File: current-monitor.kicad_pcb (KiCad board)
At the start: 4 copper layers, 70 x 58.2 mm, 152 parts, among them J201 CONN-3, J601 USB-MICROB, J602 SWD, J603 CONN-6, K201 RELAY-DPDT-EE2-SPLIT, K202 RELAY-DPDT-EE2-SPLIT, Q201 DRDC3105E6, U201 FSA1259A, U202 MAX4737EUD, U301 AD8429A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

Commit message: adjust mask clearance
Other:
- rule pad_to_mask_clearance: 0 -> 0.1
- board text added: "IN"
- board text added: "OUT"
- board text added: "sternlabs"
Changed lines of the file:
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@@
     (links 332)
     (no_connects 0)
-    (area 90.949999 59.949999 161.050001 118.250001)
+    (area 90.949999 59.949999 162.774001 118.250001)
     (thickness 1.6)
-    (drawings 8)
+    (drawings 14)
     (tracks 1240)
     (zones 0)
@@
     (zone_45_only no)
     (trace_min 0.15)
-    (segment_width 0.2)
+    (segment_width 0.3)
     (edge_width 0.1)
     (via_size 0.6)
@@
     (pad_size 1.5 0.3)
     (pad_drill 0)
-    (pad_to_mask_clearance 0)
+    (pad_to_mask_clearance 0.1)
+    (solder_mask_min_width 0.1)
     (aux_axis_origin 0 0)
     (visible_elements FFFFFF7F)
@@
       (net 2 COM))
   )
+  (gr_text sternlabs (at 98.6 116.2) (layer F.SilkS)
+    (effects (font (size 1.5 1.5) (thickness 0.15)))
+  )
+  (gr_line (start 92.4 70.8) (end 92.4 71.2) (layer F.SilkS) (width 0.3))
+  (gr_line (start 93 70.4) (end 93 71.6) (layer F.SilkS) (width 0.3))
+  (gr_line (start 93.6 70) (end 93.6 72) (layer F.SilkS) (width 0.3))
+  (gr_text OUT (at 93 74.8 270) (layer F.SilkS)
+    (effects (font (size 1.5 1.5) (thickness 0.3)))
+  )
+  (gr_text IN (at 93.2 67.6 270) (layer F.SilkS)
+    (effects (font (size 1.5 1.5) (thickness 0.3)))
+  )
   (gr_line (start 91 60) (end 91 118.2) (layer Edge.Cuts) (width 0.1))
   (gr_line (start 161 60) (end 91 60) (layer Edge.Cuts) (width 0.1))
@@
     (polygon
       (pts
-        (xy 91 60) (xy 161 60) (xy 161 118.2) (xy 91 118.4)
+        (xy 91 60) (xy 161 60) (xy 161 118.2) (xy 91 118.2)
       )
     )
@@
     (polygon
       (pts
-        (xy 148.2 110.4) (xy 143.6 105.8) (xy 143.6 104.2) (xy 147.6 104.2) (xy 150.6 109.4)
-        (xy 150.6 110.4)
+        (xy 149.6 110.4) (xy 143.6 105.8) (xy 143.6 103.4) (xy 147.6 103.4) (xy 151.8 109)
+        (xy 151.8 110.4)
       )
     )
@@
     (polygon
       (pts
-        (xy 91 60.025214) (xy 161 60.025214) (xy 161 118.225214) (xy 91 118.425214)
+        (xy 91 60) (xy 161 60) (xy 161 118.2) (xy 91 118.2)
       )
     )
@@
     (polygon
       (pts
-        (xy 90.959971 60) (xy 160.959971 60) (xy 160.959971 118.2) (xy 90.959971 118.4)
+        (xy 91 60) (xy 161 60) (xy 161 118.2) (xy 91 118.2)
       )
     )

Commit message: zone connections
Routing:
- net COM: track 111.3 -> 114.9 mm
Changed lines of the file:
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@@
     (thickness 1.6)
     (drawings 14)
-    (tracks 1240)
+    (tracks 1244)
     (zones 0)
     (modules 152)
@@
       (net 12 +3.00V))
     (pad 15 smd rect (at -5.7 3.25) (size 1.5 0.3) (layers F.Cu F.Paste F.Mask)
-      (net 2 COM))
+      (net 2 COM) (zone_connect 1))
     (pad 16 smd rect (at -5.7 3.75) (size 1.5 0.3) (layers F.Cu F.Paste F.Mask)
-      (net 2 COM))
+      (net 2 COM) (zone_connect 1))
     (pad 17 smd rect (at -3.75 5.7 90) (size 1.5 0.3) (layers F.Cu F.Paste F.Mask))
     (pad 18 smd rect (at -3.25 5.7 90) (size 1.5 0.3) (layers F.Cu F.Paste F.Mask)
@@
       (net 78 "Net-(R205-Pad2)"))
     (pad 9 smd rect (at 1.3 -3 90) (size 0.4 1.8) (layers F.Cu F.Paste F.Mask)
-      (net 2 COM))
+      (net 2 COM) (zone_connect 1))
     (pad 10 smd rect (at 0.65 -3 90) (size 0.4 1.8) (layers F.Cu F.Paste F.Mask)
-      (net 2 COM))
+      (net 2 COM) (zone_connect 1))
     (pad 11 smd rect (at 0 -3 90) (size 0.4 1.8) (layers F.Cu F.Paste F.Mask)
       (net 77 "Net-(R204-Pad2)"))
@@
   (segment (start 102.75 87.8) (end 102.5 87.55) (width 0.4) (layer F.Cu) (net 1) (status 30))
   (segment (start 102.5 85.25) (end 103.05 84.7) (width 0.4) (layer F.Cu) (net 1) (status 30))
+  (segment (start 145.8 66.7) (end 144.468202 66.7) (width 0.4) (layer F.Cu) (net 2))
+  (segment (start 144.468202 66.7) (end 144.168202 67) (width 0.4) (layer F.Cu) (net 2))
+  (segment (start 145.8 67.35) (end 144.5 67.35) (width 0.4) (layer F.Cu) (net 2))
+  (segment (start 144.5 67.35) (end 144.15 67) (width 0.4) (layer F.Cu) (net 2))
+  (segment (start 145.8 67.35) (end 146.95 67.35) (width 0.4) (layer F.Cu) (net 2))
+  (segment (start 146.95 67.35) (end 147 67.4) (width 0.4) (layer F.Cu) (net 2))
+  (segment (start 145.8 66.7) (end 146.9 66.7) (width 0.4) (layer F.Cu) (net 2))
+  (segment (start 146.9 66.7) (end 147 66.8) (width 0.4) (layer F.Cu) (net 2))
   (segment (start 140.3 97.5) (end 140.3 98.3) (width 0.2) (layer F.Cu) (net 2))
   (segment (start 140.3 98.3) (end 140.2 98.4) (width 0.2) (layer F.Cu) (net 2))
@@
   (segment (start 138.8 65.4) (end 139.6 65.4) (width 0.5) (layer F.Cu) (net 2) (status 10))
   (via (at 139.6 65.4) (size 0.6) (drill 0.3) (layers F.Cu B.Cu) (net 2))
-  (segment (start 145.8 66.7) (end 146.9 66.7) (width 0.3) (layer F.Cu) (net 2) (status 10))
-  (segment (start 146.9 66.7) (end 147 66.8) (width 0.3) (layer F.Cu) (net 2))
   (via (at 147 66.8) (size 0.6) (drill 0.3) (layers F.Cu B.Cu) (net 2))
-  (segment (start 145.8 67.35) (end 146.95 67.35) (width 0.3) (layer F.Cu) (net 2) (status 10))
-  (segment (start 146.95 67.35) (end 147 67.4) (width 0.3) (layer F.Cu) (net 2))
   (via (at 147 67.4) (size 0.6) (drill 0.3) (layers F.Cu B.Cu) (net 2))
   (segment (start 151.8 66.05) (end 150.65 66.05) (width 0.3) (layer F.Cu) (net 2) (status 10))
@@
   (segment (start 131.7 71.273) (end 131.71 71.283) (width 1) (layer F.Cu) (net 73) (status 30))
   (segment (start 131.71 70.338) (end 131.71 71.283) (width 1) (layer F.Cu) (net 73) (status 30))
+  (segment (start 99.8 74.5) (end 100.1 74.5) (width 1) (layer F.Cu) (net 74))
+  (segment (start 100.1 74.5) (end 102.8 71.8) (width 1) (layer F.Cu) (net 74))
+  (segment (start 106.865999 69.083999) (end 109.065 71.283) (width 1) (layer F.Cu) (net 74))
+  (segment (start 102.8 71.8) (end 102.8 70.709798) (width 1) (layer F.Cu) (net 74))
+  (segment (start 102.8 70.709798) (end 104.425799 69.083999) (width 1) (layer F.Cu) (net 74))
+  (segment (start 104.425799 69.083999) (end 106.865999 69.083999) (width 1) (layer F.Cu) (net 74))
   (segment (start 106.2 75.2) (end 106 75.4) (width 0.5) (layer F.Cu) (net 74))
   (segment (start 107.8 75.2) (end 106.2 75.2) (width 0.5) (layer F.Cu) (net 74))
@@
   (segment (start 103.5 71.1) (end 100.1 74.5) (width 1) (layer B.Cu) (net 74))
   (segment (start 100.1 74.5) (end 99.8 74.5) (width 1) (layer B.Cu) (net 74))
-  (segment (start 99.8 74.5) (end 100.1 74.5) (width 1) (layer F.Cu) (net 74))
-  (segment (start 100.1 74.5) (end 102.1 72.5) (width 1) (layer F.Cu) (net 74))
-  (segment (start 102.1 72.5) (end 102.1 71.409798) (width 1) (layer F.Cu) (net 74))
-  (segment (start 104.425799 69.083999) (end 106.865999 69.083999) (width 1) (layer F.Cu) (net 74))
-  (segment (start 102.1 71.409798) (end 104.425799 69.083999) (width 1) (layer F.Cu) (net 74))
   (segment (start 129.4 74) (end 129.4 71.513) (width 0.5) (layer F.Cu) (net 74))
   (segment (start 129.4 71.513) (end 129.17 71.283) (width 0.5) (layer F.Cu) (net 74))
   (segment (start 129.1 69.2) (end 127.2 71.1) (width 1) (layer B.Cu) (net 74))
-  (segment (start 106.865999 69.083999) (end 109.065 71.283) (width 1) (layer F.Cu) (net 74))
   (segment (start 109.065 71.283) (end 110.62 71.283) (width 1) (layer F.Cu) (net 74) (status 20))
   (segment (start 129.17 71.283) (end 129.17 69.27) (width 1) (layer F.Cu) (net 74) (status 10))
@@
     (connect_pads yes (clearance 0.2))
     (min_thickness 0.254)
-    (fill yes (arc_segments 32) (thermal_gap 0.508) (thermal_bridge_width 0.508))
+    (fill yes (arc_segments 32) (thermal_gap 0.2) (thermal_bridge_width 0.508))
     (polygon
       (pts

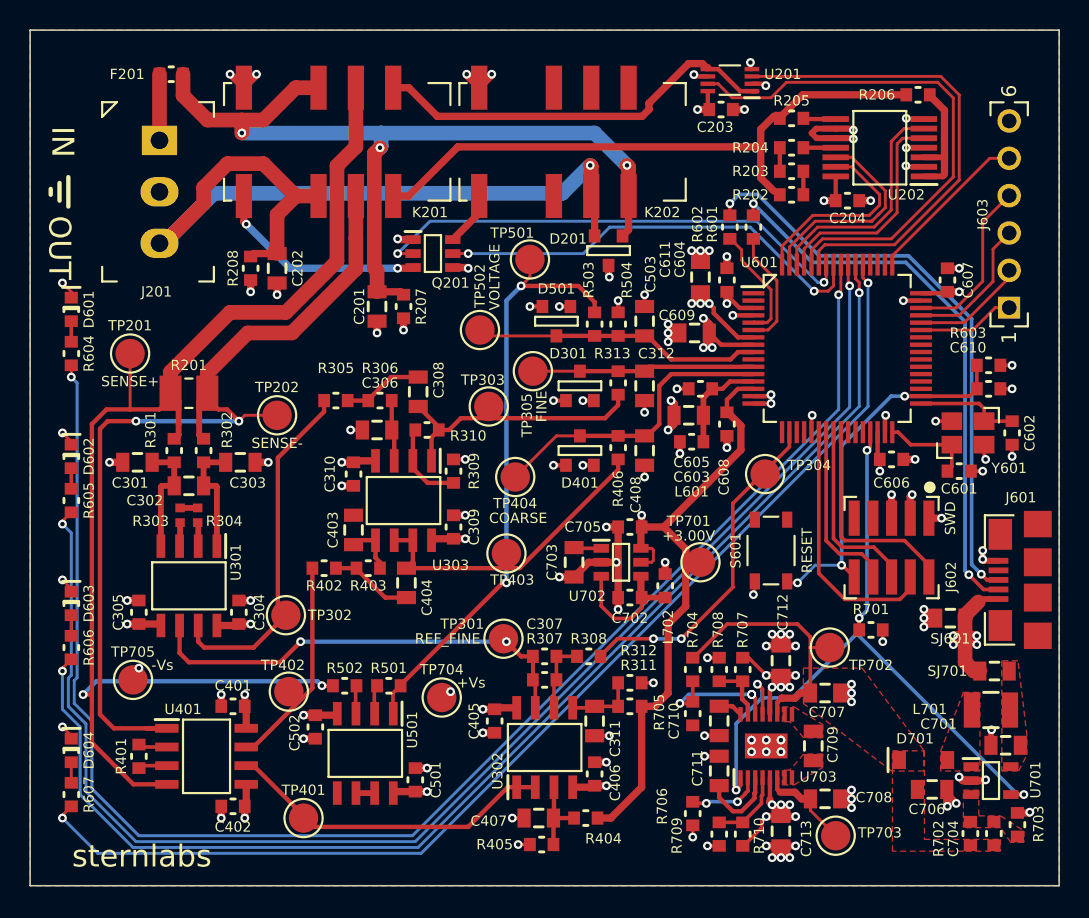
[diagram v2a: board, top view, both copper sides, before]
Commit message: move Q201 to the east
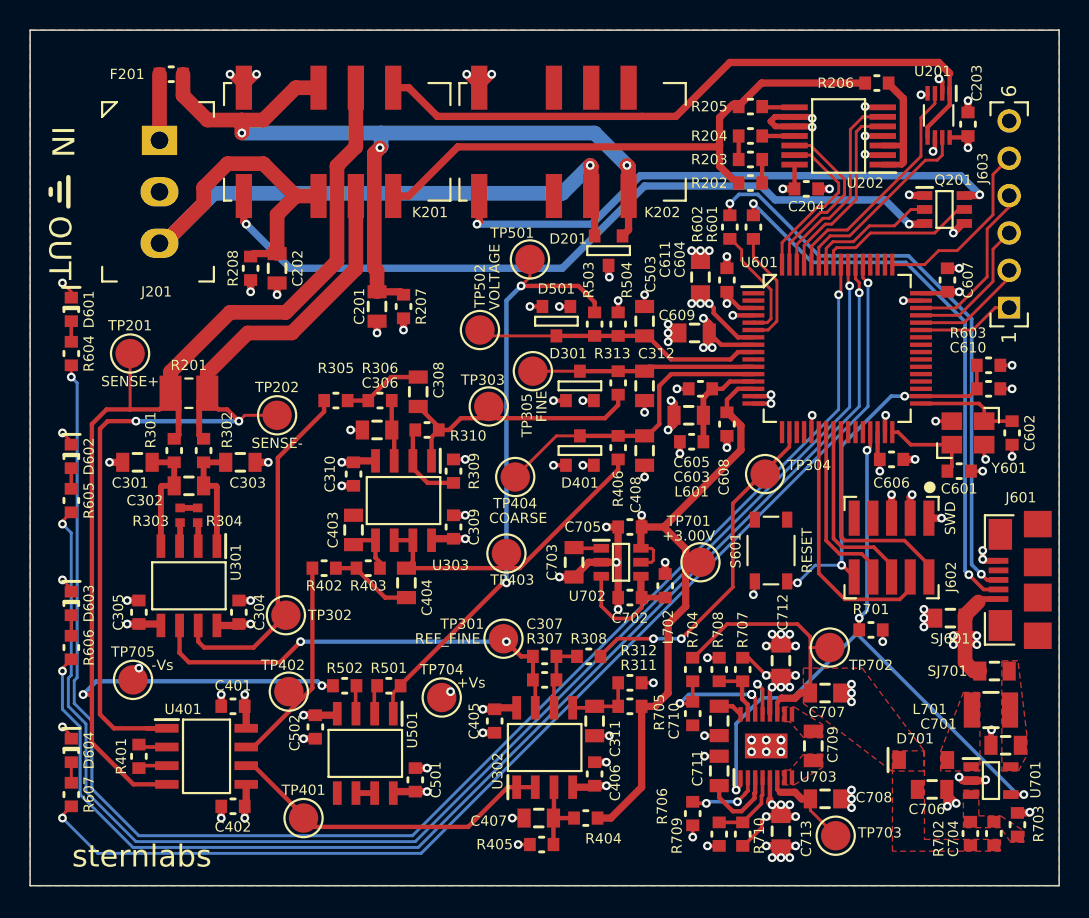
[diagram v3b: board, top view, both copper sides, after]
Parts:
- moved Q201 34.9 mm to (153.2, 72.2)
- moved C203 16.8 mm to (154.8, 66.4), turned to 180 degrees
- moved U201 14.4 mm to (152.8, 65.8), turned to 180 degrees
- moved R206 2.91 mm to (148.6, 63.6)
- moved R202 2.91 mm to (140.0, 70.4)
- moved R203 2.91 mm to (140.0, 68.8)
- moved R204 2.91 mm to (140.0, 67.2)
- moved R205 2.91 mm to (140.0, 65.2)
- moved U202 2.91 mm to (146.0, 67.2)
- moved C204 2.91 mm to (143.8, 70.8)
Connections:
- U601 pad 59: /In/Out, Shunt, Calibration/CALIBRATE_3V -> /In/Out, Shunt, Calibration/CALIBRATE_5V
- U601 pad 60: /In/Out, Shunt, Calibration/CALIBRATE_5V -> /In/Out, Shunt, Calibration/CALIBRATE_3V
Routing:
- net Net-(K201-Pad12): track 14.6 -> 52.8 mm
- net Net-(K202-Pad12): track 3.71 -> 39.2 mm, vias 0 -> 2
- net /In/Out, Shunt, Calibration/RELAY_CALIBRATE: track 34.0 -> 8.90 mm, vias 2 -> 0
- net /In/Out, Shunt, Calibration/CALIBRATE_5V: track 36.1 -> 13.4 mm
- net /In/Out, Shunt, Calibration/RELAY_INOUT_SHORT: track 30.0 -> 11.0 mm, vias 2 -> 0
- net Net-(K201-Pad5): track 28.4 -> 46.2 mm
- net /In/Out, Shunt, Calibration/CALIBRATE_3V: track 32.9 -> 15.9 mm
- net +5V: track 54.1 -> 39.4 mm
- net +3.00V: track 91.0 -> 101.9 mm
- net +3V3: track 107.7 -> 101.2 mm
- net Net-(K201-Pad8): track 41.7 -> 38.9 mm
- net /In/Out, Shunt, Calibration/CALIBRATE_3uA: track 14.4 -> 12.0 mm
- net /In/Out, Shunt, Calibration/CALIBRATE_300uA: track 15.9 -> 13.5 mm
- net /In/Out, Shunt, Calibration/CALIBRATE_30mA_2: track 15.1 -> 12.7 mm
- net /In/Out, Shunt, Calibration/CALIBRATE_30mA: track 13.5 -> 11.2 mm
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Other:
- rule pad_to_mask_clearance: 0.1 -> 0.049

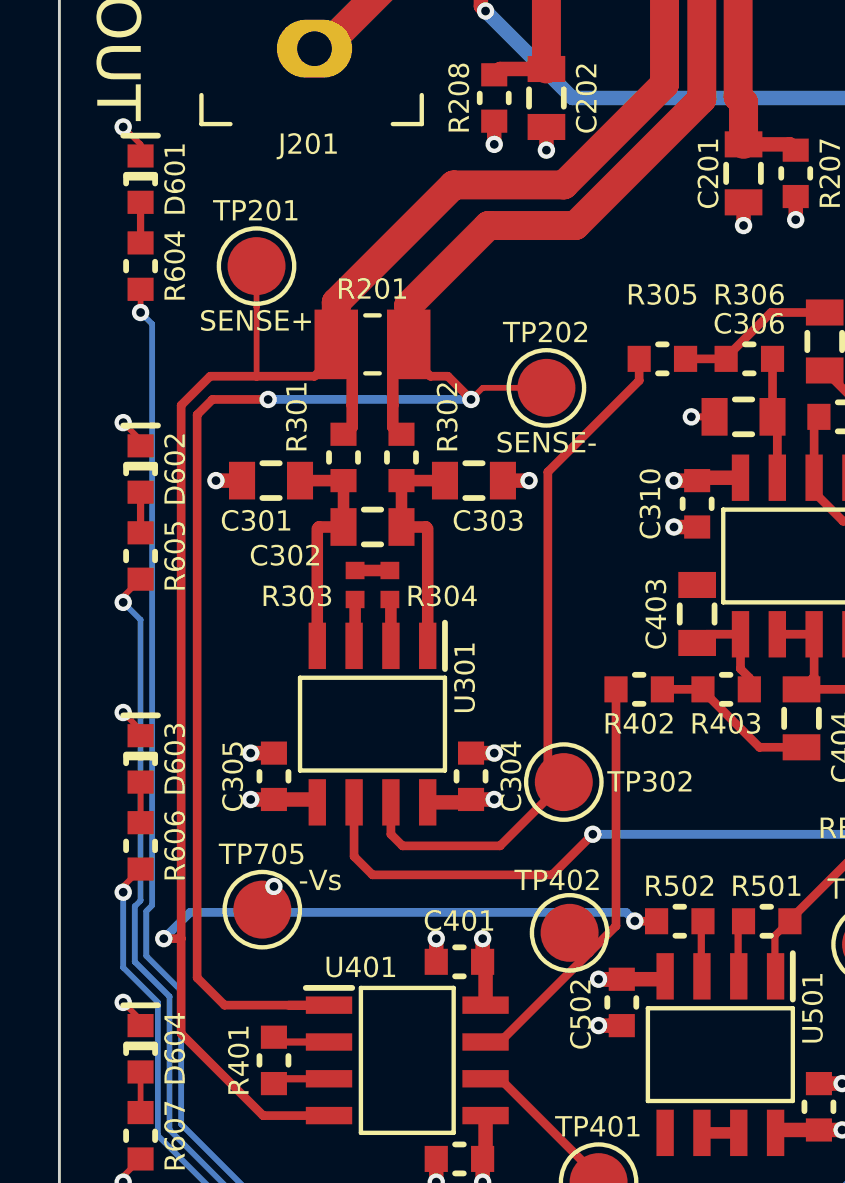
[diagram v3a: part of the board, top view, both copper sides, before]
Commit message: use rfi filter for all inputs
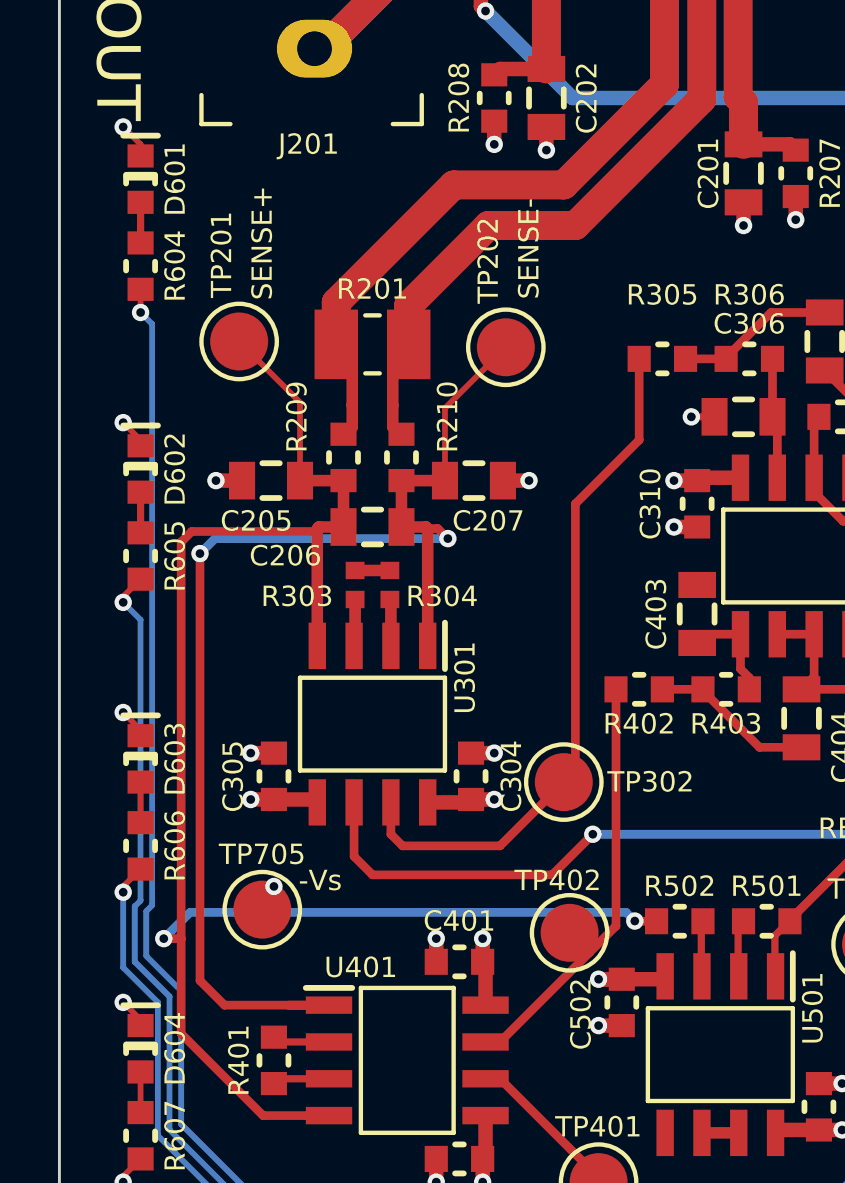
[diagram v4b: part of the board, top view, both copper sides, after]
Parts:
- moved TP201 2.67 mm to (97.2, 84.6)
- moved TP202 1.98 mm to (106.4, 84.8)
- renumbered C301 to C205, C302 to C206, C303 to C207, R301 to R209, R302 to R210
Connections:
- C205 pad 1: Net-(C301-Pad1) -> SENSE+
- C206 pad 1: Net-(C301-Pad1) -> SENSE+
- C206 pad 2: Net-(C302-Pad2) -> SENSE-
- C207 pad 1: Net-(C302-Pad2) -> SENSE-
- K201 pad 4: SENSE+ -> Net-(K201-Pad4)
- K201 pad 9: SENSE- -> Net-(K201-Pad9)
- R201 pad 1: SENSE+ -> Net-(K201-Pad4)
- R201 pad 2: SENSE- -> Net-(K201-Pad9)
- R209 pad 1: SENSE+ -> Net-(K201-Pad4)
- R209 pad 2: Net-(C301-Pad1) -> SENSE+
- R210 pad 1: SENSE- -> Net-(K201-Pad9)
- R210 pad 2: Net-(C302-Pad2) -> SENSE-
- U301 pad 1: Net-(C302-Pad2) -> SENSE-
- U301 pad 4: Net-(C301-Pad1) -> SENSE+
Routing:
- net Net-(K201-Pad4): track 0.00 -> 32.4 mm
- net SENSE+: track 89.2 -> 59.8 mm
- net Net-(K201-Pad9): track 0.00 -> 23.2 mm
- net SENSE-: track 64.2 -> 44.0 mm
- net Net-(C302-Pad2): track 7.97 -> 0.00 mm
- net Net-(C301-Pad1): track 7.97 -> 0.00 mm
